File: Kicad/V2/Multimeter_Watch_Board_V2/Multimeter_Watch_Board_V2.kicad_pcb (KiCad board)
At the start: 4 copper layers, 46 x 42 mm, 50 parts, among them J1 S3B-PH-K-S(LF)(SN), J2 S3B-PH-K-S(LF)(SN), J3 S3B-PH-K-S(LF)(SN), J6 51281-1294, J7 Conn_01x11_Female, J8 Conn_01x11_Female, Q1 A03400A N-MOS, U1 PCF85163-SO08, U2 AD8592, Y1 32kHz

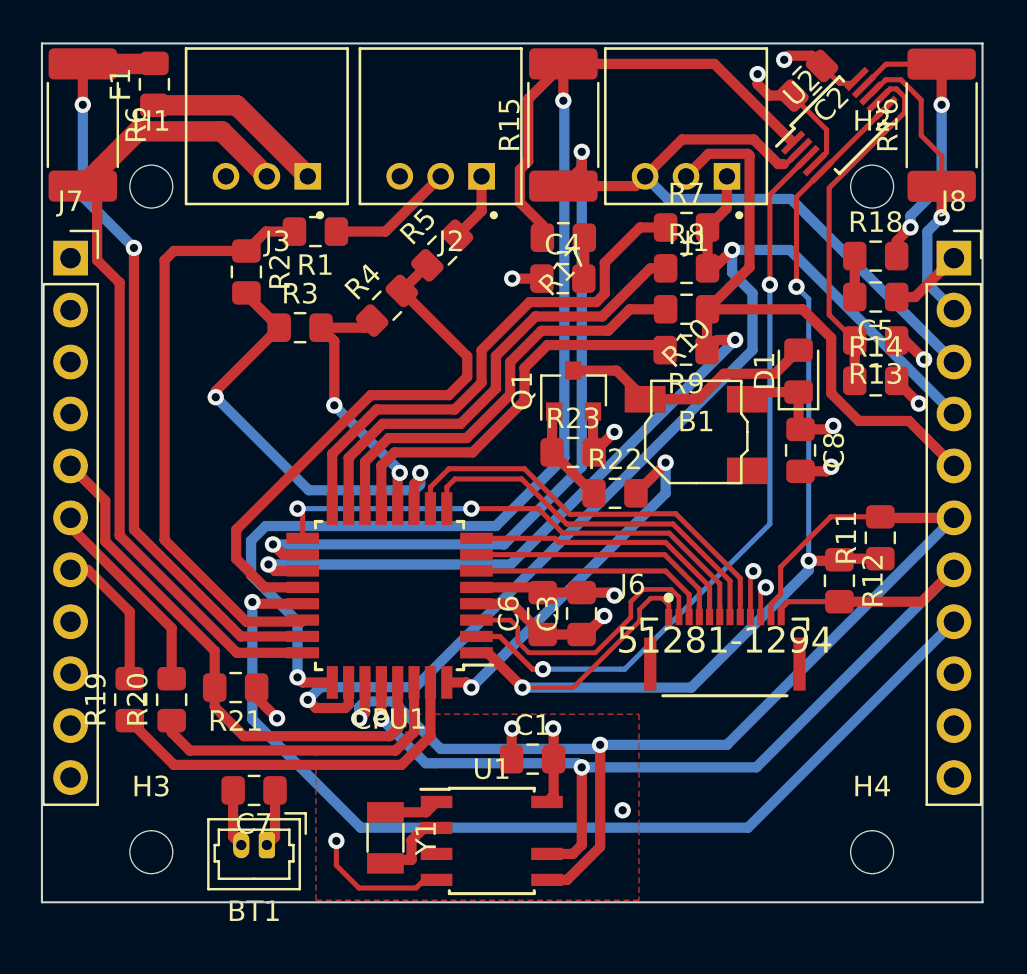
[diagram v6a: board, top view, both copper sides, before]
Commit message: silkscreen improvements (bottom board)
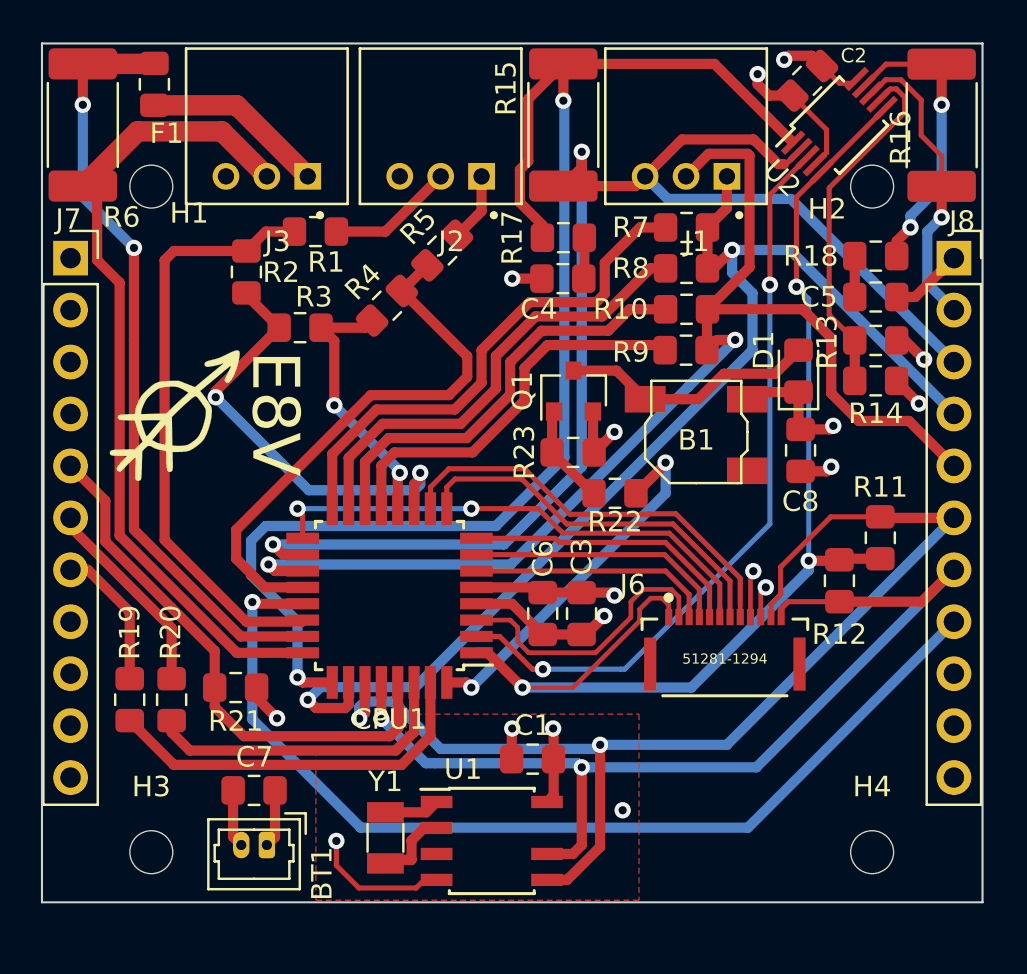
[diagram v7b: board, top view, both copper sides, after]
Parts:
- added G***: LOGO, Multimeter_Watch_Custom_Footprints:nouth_signature, F.Cu at (108.5, 76.2)
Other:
- board text added: "E8V"

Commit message: displayboard layout for V2
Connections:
- net /ADC11 renamed /PB5
- J6 pad 9: /VCC -> /GND
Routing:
- net /VCC: track 30.2 -> 27.9 mm, vias 7 -> 6
